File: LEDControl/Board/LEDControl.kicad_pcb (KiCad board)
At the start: 2 copper layers, 100 x 40 mm, 21 parts, among them IC1 ATMEGA88PA-M, P1 CONN_12V, P2 CONN_LED, P3 CONN_ISP, P4 CONN_01X01, Q1 IRLZ34N, Q2 IRLZ34N, Q3 IRLZ34N, U1 LM2931AZ-3.3/5.0, U2 RFM69CW

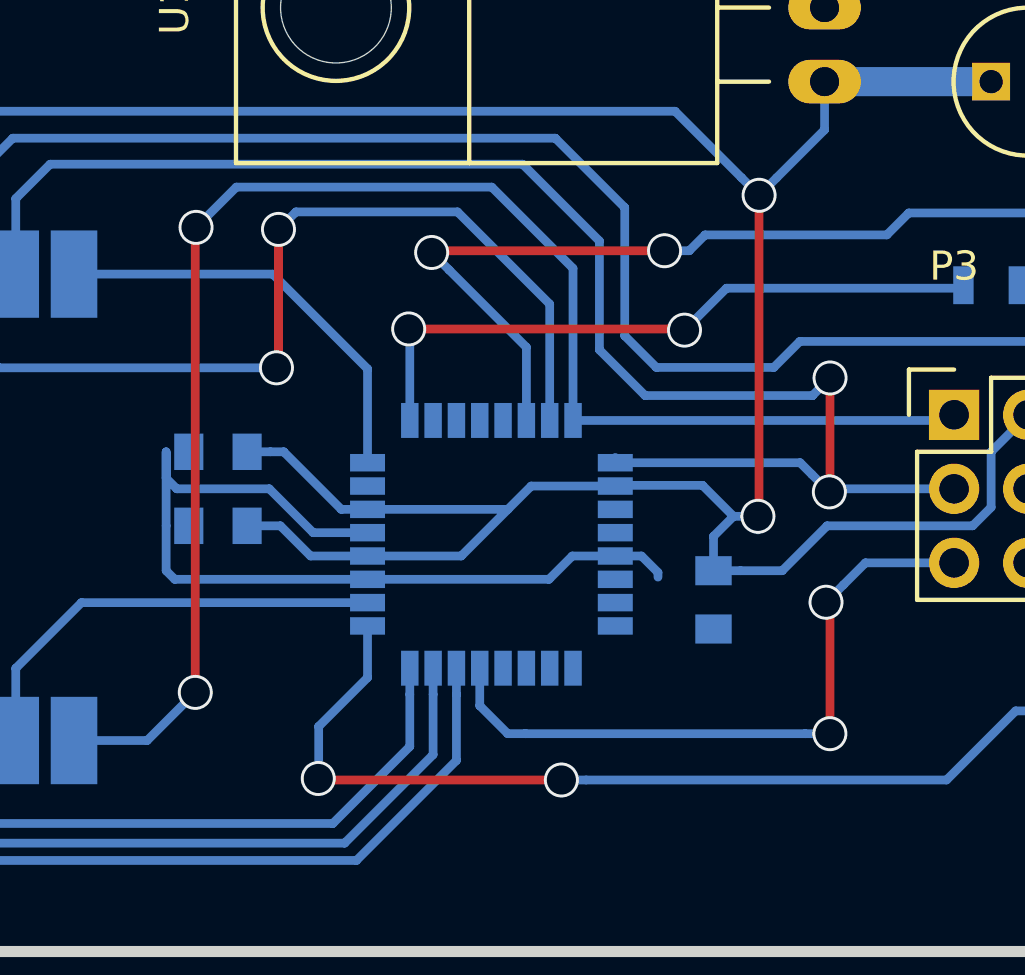
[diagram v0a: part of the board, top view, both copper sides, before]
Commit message: PiShield neu angelegt
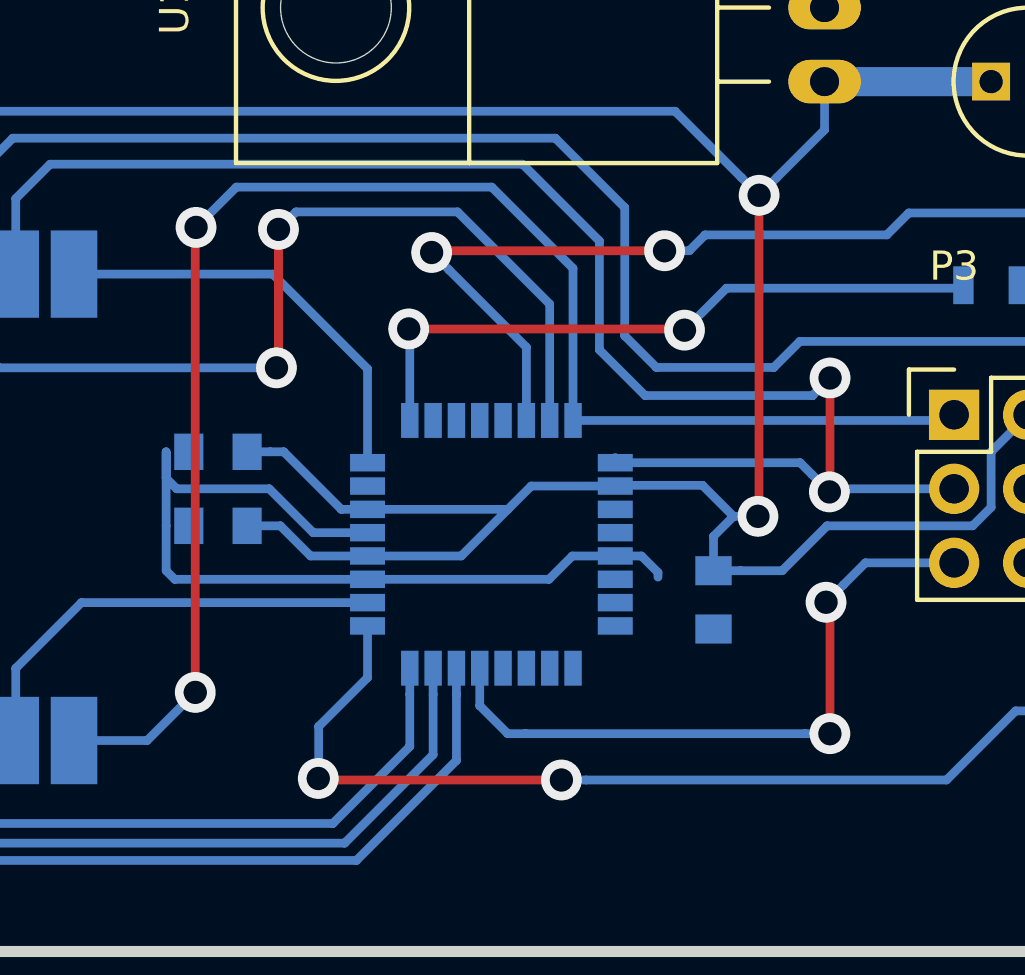
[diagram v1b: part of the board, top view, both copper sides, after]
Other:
- net class Default: via_dia 1.2 -> 1.4; via_drill 1 -> 0.8
- net class Power: via_dia 1.2 -> 1.4; via_drill 1 -> 0.8
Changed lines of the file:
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@@
     (segment_width 0.2)
     (edge_width 0.15)
-    (via_size 1.2)
-    (via_drill 1)
+    (via_size 1.4)
+    (via_drill 0.8)
     (via_min_size 0.4)
     (via_min_drill 0.3)
@@
     (clearance 0.25)
     (trace_width 0.25)
-    (via_dia 1.2)
-    (via_drill 1)
+    (via_dia 1.4)
+    (via_drill 0.8)
     (uvia_dia 0.3)
     (uvia_drill 0.1)
@@
     (clearance 0.25)
     (trace_width 1)
-    (via_dia 1.2)
-    (via_drill 1)
+    (via_dia 1.4)
+    (via_drill 0.8)
     (uvia_dia 0.3)
     (uvia_drill 0.1)
@@
   (segment (start 136.184576 110.758868) (end 136.144522 110.798922) (width 0.3) (layer F.Cu) (net 3))
   (segment (start 136.184576 99.784195) (end 136.184576 110.758868) (width 0.3) (layer F.Cu) (net 3))
-  (via (at 136.144522 110.798922) (size 1.2) (drill 1) (layers F.Cu B.Cu) (net 3))
+  (via (at 136.144522 110.798922) (size 1.4) (drill 0.8) (layers F.Cu B.Cu) (net 3))
   (segment (start 136.784575 99.184196) (end 136.184576 99.784195) (width 0.3) (layer B.Cu) (net 3))
   (segment (start 138.43 95.885) (end 138.43 97.538771) (width 0.3) (layer B.Cu) (net 3))
@@
   (segment (start 135.584577 99.184196) (end 136.184576 99.784195) (width 0.3) (layer B.Cu) (net 3))
   (segment (start 102.854 96.901) (end 133.301381 96.901) (width 0.3) (layer B.Cu) (net 3))
-  (via (at 136.184576 99.784195) (size 1.2) (drill 1) (layers F.Cu B.Cu) (net 3))
+  (via (at 136.184576 99.784195) (size 1.4) (drill 0.8) (layers F.Cu B.Cu) (net 3) (status 1000000))
   (segment (start 102.6795 102.489) (end 102.6795 97.2025) (width 0.25) (layer B.Cu) (net 3))
   (segment (start 102.6795 97.2025) (end 102.854 97.028) (width 0.25) (layer B.Cu) (net 3))
@@
   (segment (start 119.694628 105.634917) (end 119.625817 105.703728) (width 0.3) (layer F.Cu) (net 7))
   (segment (start 119.694628 100.954306) (end 119.694628 105.634917) (width 0.3) (layer F.Cu) (net 7))
-  (via (at 119.625817 105.703728) (size 1.2) (drill 1) (layers F.Cu B.Cu) (net 7))
-  (via (at 119.694628 100.954306) (size 1.2) (drill 1) (layers F.Cu B.Cu) (net 7))
+  (via (at 119.625817 105.703728) (size 1.4) (drill 0.8) (layers F.Cu B.Cu) (net 7))
+  (via (at 119.694628 100.954306) (size 1.4) (drill 0.8) (layers F.Cu B.Cu) (net 7))
   (segment (start 129.8 107.51) (end 129.8 102.291508) (width 0.3) (layer B.Cu) (net 8))
   (segment (start 129.8 102.291508) (end 127.012312 99.50382) (width 0.3) (layer B.Cu) (net 8))
@@
   (segment (start 142.276417 107.51) (end 142.471417 107.315) (width 0.3) (layer B.Cu) (net 8))
   (segment (start 116.84 100.91216) (end 116.866662 100.885498) (width 0.3) (layer F.Cu) (net 8))
-  (via (at 116.866662 100.885498) (size 1.2) (drill 1) (layers F.Cu B.Cu) (net 8))
+  (via (at 116.866662 100.885498) (size 1.4) (drill 0.8) (layers F.Cu B.Cu) (net 8))
   (segment (start 116.84 116.84) (end 116.84 100.91216) (width 0.3) (layer F.Cu) (net 8))
   (segment (start 112.67948 118.491) (end 115.189 118.491) (width 0.3) (layer B.Cu) (net 8) (status 10))
   (segment (start 115.189 118.491) (end 116.84 116.84) (width 0.3) (layer B.Cu) (net 8))
-  (via (at 116.84 116.84) (size 1.2) (drill 1) (layers F.Cu B.Cu) (net 8))
+  (via (at 116.84 116.84) (size 1.4) (drill 0.8) (layers F.Cu B.Cu) (net 8))
   (segment (start 110.6805 102.489) (end 110.6805 99.897577) (width 0.3) (layer B.Cu) (net 9))
   (segment (start 110.6805 99.897577) (end 111.860152 98.717925) (width 0.3) (layer B.Cu) (net 9))
@@
   (segment (start 138.619084 109.936867) (end 138.594957 109.960994) (width 0.3) (layer F.Cu) (net 9))
   (segment (start 138.619084 106.05246) (end 138.619084 109.936867) (width 0.3) (layer F.Cu) (net 9))
-  (via (at 138.594957 109.960994) (size 1.2) (drill 1) (layers F.Cu B.Cu) (net 9))
+  (via (at 138.594957 109.960994) (size 1.4) (drill 0.8) (layers F.Cu B.Cu) (net 9))
   (segment (start 142.875 109.855) (end 138.700951 109.855) (width 0.3) (layer B.Cu) (net 9))
   (segment (start 137.994958 109.360995) (end 138.594957 109.960994) (width 0.3) (layer B.Cu) (net 9))
   (segment (start 137.593963 108.96) (end 137.994958 109.360995) (width 0.3) (layer B.Cu) (net 9))
-  (via (at 138.619084 106.05246) (size 1.2) (drill 1) (layers F.Cu B.Cu) (net 9))
+  (via (at 138.619084 106.05246) (size 1.4) (drill 0.8) (layers F.Cu B.Cu) (net 9))
   (segment (start 131.25 108.96) (end 131.25 108.78) (width 0.3) (layer B.Cu) (net 9) (status 30))
   (segment (start 126.6 116.01) (end 126.6 117.296619) (width 0.3) (layer B.Cu) (net 10))
@@
   (segment (start 138.613449 118.256721) (end 138.613449 113.879586) (width 0.3) (layer F.Cu) (net 10))
   (segment (start 138.613449 113.879586) (end 138.480808 113.746945) (width 0.3) (layer F.Cu) (net 10))
-  (via (at 138.480808 113.746945) (size 1.2) (drill 1) (layers F.Cu B.Cu) (net 10))
-  (via (at 138.613449 118.256721) (size 1.2) (drill 1) (layers F.Cu B.Cu) (net 10))
+  (via (at 138.480808 113.746945) (size 1.4) (drill 0.8) (layers F.Cu B.Cu) (net 10))
+  (via (at 138.613449 118.256721) (size 1.4) (drill 0.8) (layers F.Cu B.Cu) (net 10))
   (segment (start 149.86 100.391) (end 141.319932 100.391) (width 0.3) (layer B.Cu) (net 11))
   (segment (start 141.319932 100.391) (end 140.5671 101.143832) (width 0.3) (layer B.Cu) (net 11))
@@
   (segment (start 125.009634 101.686739) (end 124.949554 101.746819) (width 0.3) (layer F.Cu) (net 11))
   (segment (start 132.940238 101.686739) (end 125.009634 101.686739) (width 0.3) (layer F.Cu) (net 11))
-  (via (at 124.949554 101.746819) (size 1.2) (drill 1) (layers F.Cu B.Cu) (net 11))
-  (via (at 132.940238 101.686739) (size 1.2) (drill 1) (layers F.Cu B.Cu) (net 11))
+  (via (at 124.949554 101.746819) (size 1.4) (drill 0.8) (layers F.Cu B.Cu) (net 11))
+  (via (at 132.940238 101.686739) (size 1.4) (drill 0.8) (layers F.Cu B.Cu) (net 11))
   (segment (start 122.75 114.56) (end 122.75 116.332506) (width 0.3) (layer B.Cu) (net 12))
   (segment (start 122.75 116.332506) (end 121.073419 118.009087) (width 0.3) (layer B.Cu) (net 12))
@@
   (segment (start 121.112107 119.845496) (end 121.059902 119.793291) (width 0.3) (layer F.Cu) (net 12))
   (segment (start 129.400862 119.845496) (end 121.112107 119.845496) (width 0.3) (layer F.Cu) (net 12))
-  (via (at 121.059902 119.793291) (size 1.2) (drill 1) (layers F.Cu B.Cu) (net 12))
+  (via (at 121.059902 119.793291) (size 1.4) (drill 0.8) (layers F.Cu B.Cu) (net 12))
   (segment (start 147.64 117.475) (end 144.985645 117.475) (width 0.3) (layer B.Cu) (net 12))
   (segment (start 144.985645 117.475) (end 142.615149 119.845496) (width 0.3) (layer B.Cu) (net 12))
   (segment (start 142.615149 119.845496) (end 130.24939 119.845496) (width 0.3) (layer B.Cu) (net 12))
   (segment (start 130.24939 119.845496) (end 129.400862 119.845496) (width 0.3) (layer B.Cu) (net 12))
-  (via (at 129.400862 119.845496) (size 1.2) (drill 1) (layers F.Cu B.Cu) (net 12))
+  (via (at 129.400862 119.845496) (size 1.4) (drill 0.8) (layers F.Cu B.Cu) (net 12))
   (segment (start 133.624845 104.41184) (end 135.064227 102.972458) (width 0.3) (layer B.Cu) (net 13))
   (segment (start 135.064227 102.972458) (end 142.981817 102.972458) (width 0.3) (layer B.Cu) (net 13))
@@
   (segment (start 133.582335 104.36933) (end 133.624845 104.41184) (width 0.3) (layer F.Cu) (net 13))
   (segment (start 124.162008 104.36933) (end 133.582335 104.36933) (width 0.3) (layer F.Cu) (net 13))
-  (via (at 133.624845 104.41184) (size 1.2) (drill 1) (layers F.Cu B.Cu) (net 13))
+  (via (at 133.624845 104.41184) (size 1.4) (drill 0.8) (layers F.Cu B.Cu) (net 13))
   (segment (start 124.2 104.407322) (end 124.162008 104.36933) (width 0.3) (layer B.Cu) (net 13))
   (segment (start 124.2 107.51) (end 124.2 104.407322) (width 0.3) (layer B.Cu) (net 13) (status 10))
-  (via (at 124.162008 104.36933) (size 1.2) (drill 1) (layers F.Cu B.Cu) (net 13))
+  (via (at 124.162008 104.36933) (size 1.4) (drill 0.8) (layers F.Cu B.Cu) (net 13))
   (segment (start 92.71 115.57) (end 96.52 115.57) (width 0.3) (layer B.Cu) (net 14) (status 10))
   (segment (start 100.68052 111.40948) (end 100.68052 102.49154) (width 0.3) (layer B.Cu) (net 14) (status 20))
